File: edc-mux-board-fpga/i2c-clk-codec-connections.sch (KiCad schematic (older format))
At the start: 4 parts

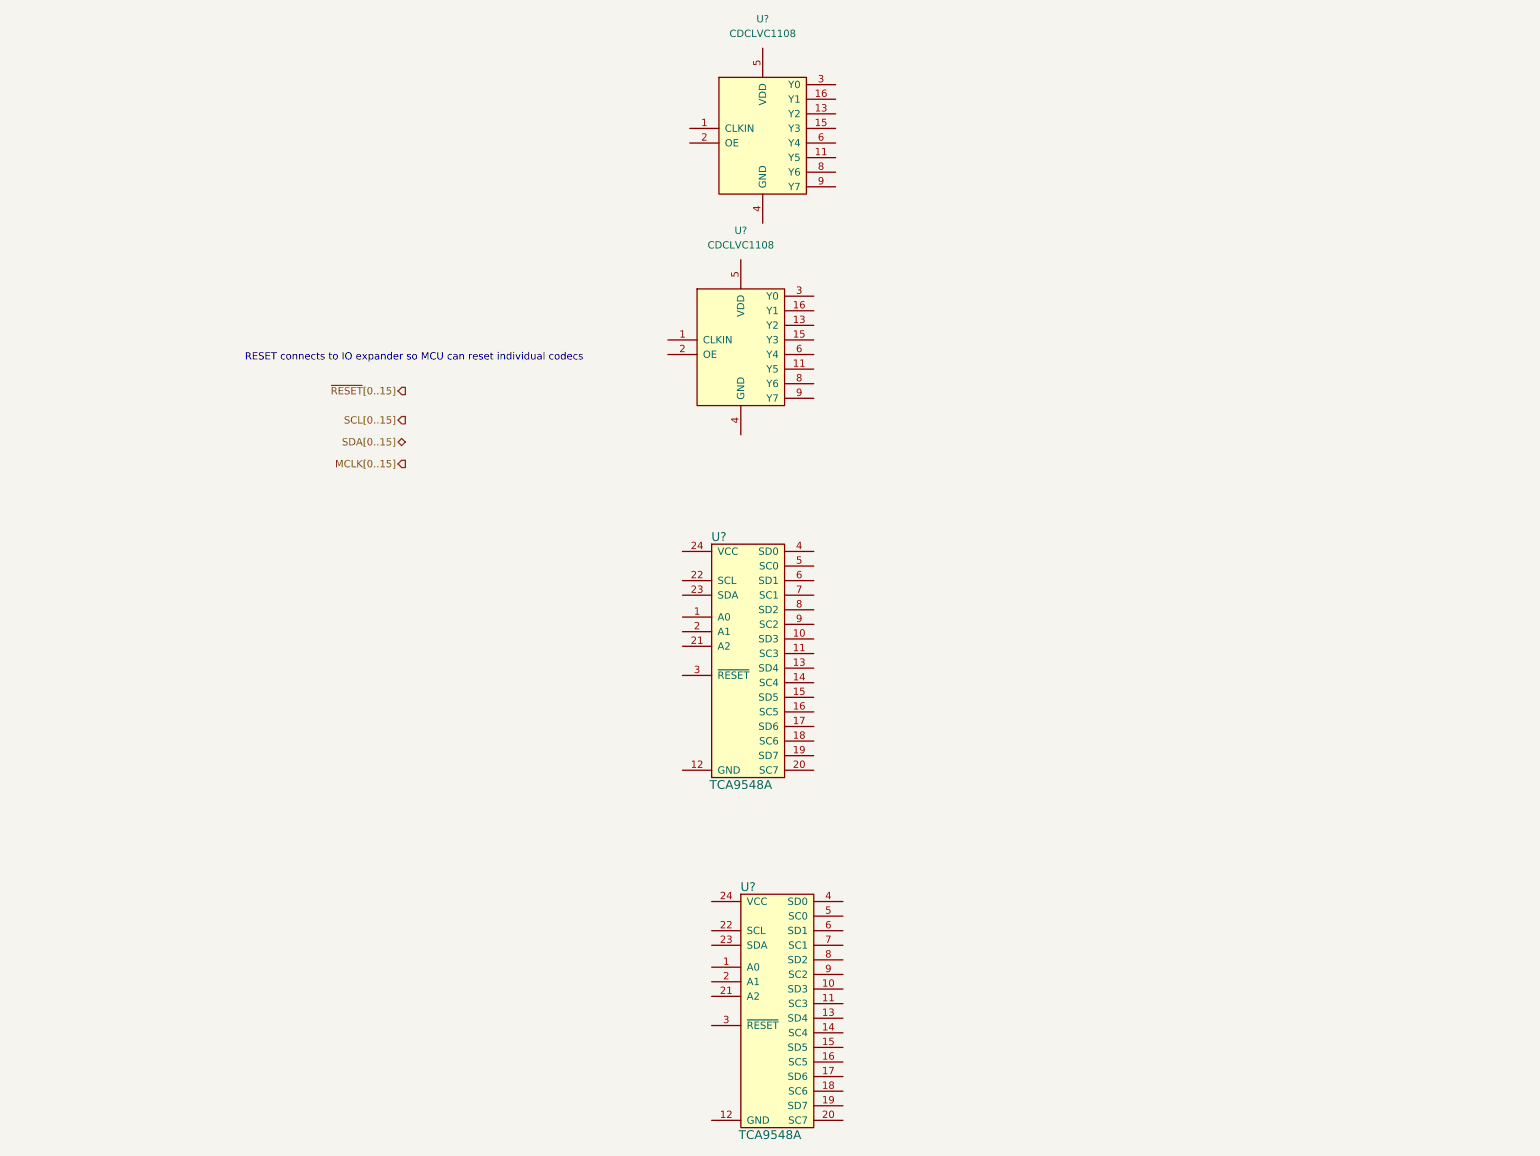
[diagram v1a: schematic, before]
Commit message: connected up mclks for codecs
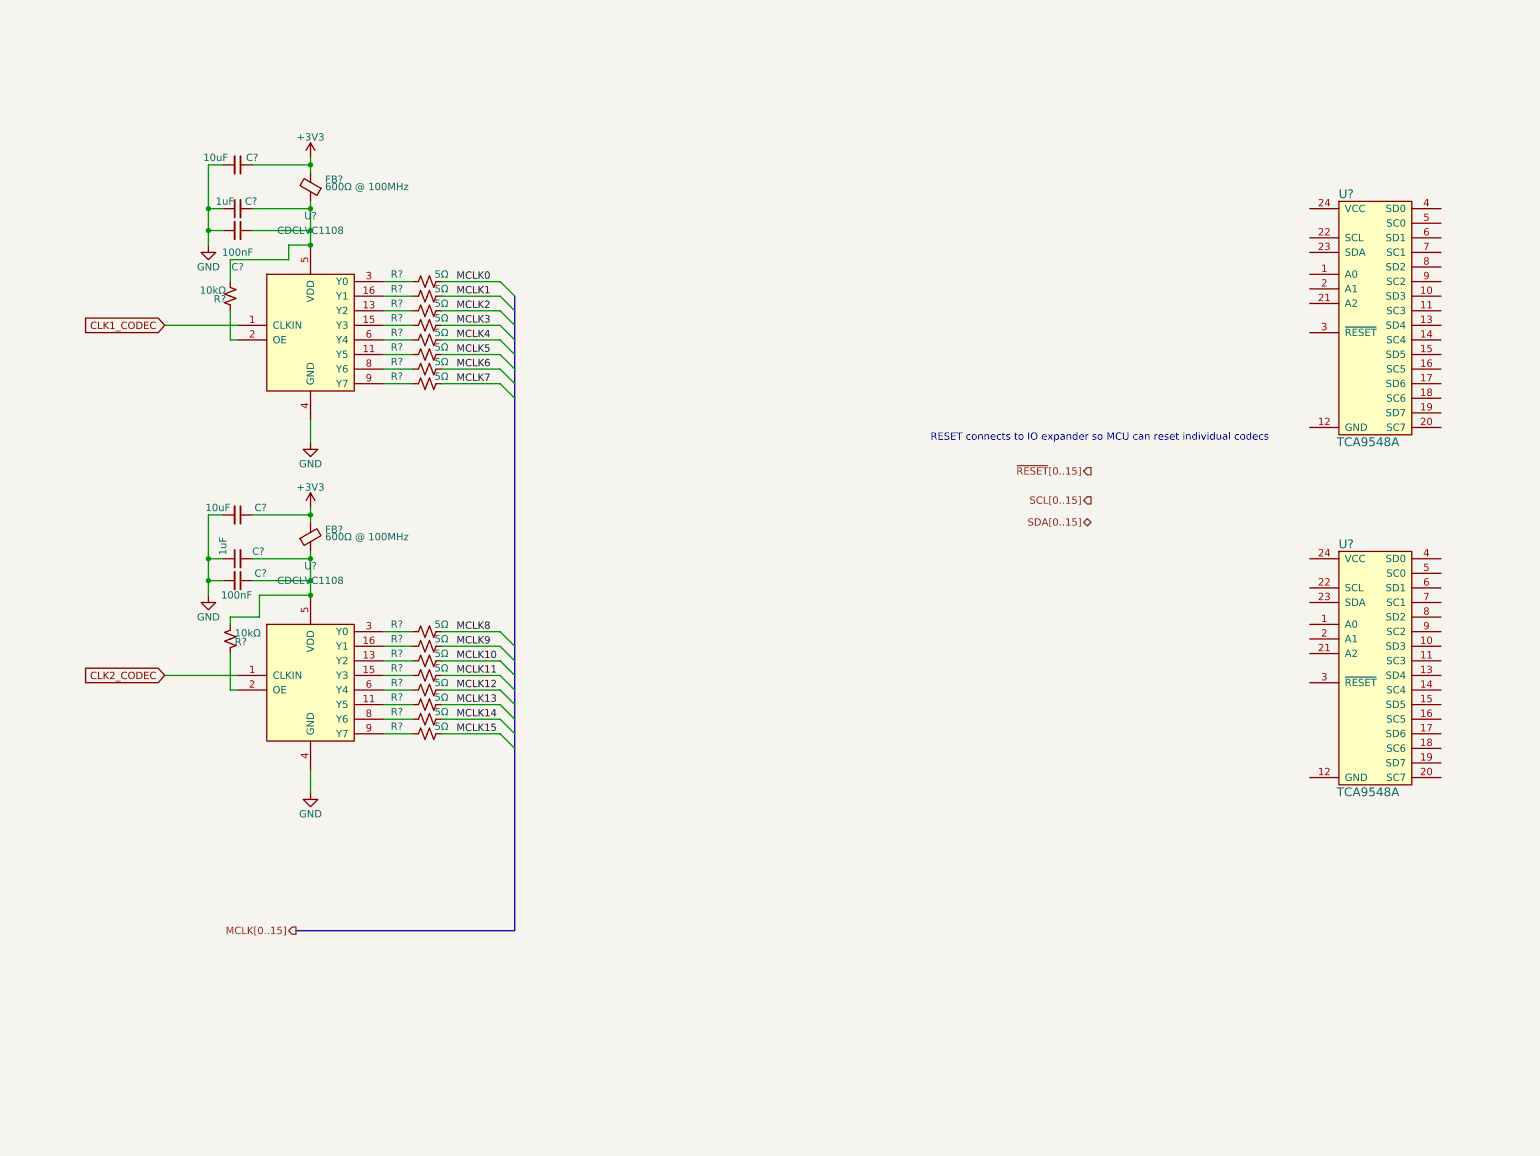
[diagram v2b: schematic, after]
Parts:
- added C? (x2): 1uF, Capacitor_SMD:C_0603_1608Metric, symbol Device:C_Small
- added C? (x2): 10uF, Capacitor_SMD:C_1206_3216Metric, symbol Device:C_Small
- added C? (x2): 100nF, Capacitor_SMD:C_0603_1608Metric, symbol Device:C_Small
- added FB? (x2): 600Ω @ 100MHz, Capacitor_SMD:C_0805_2012Metric, symbol Device:Ferrite_Bead_Small
- added R? (x2): 10kΩ, symbol Device:R_Small_US
- added R? (x16): 5Ω, symbol Device:R_Small_US
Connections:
- net CLK1_CODEC: now reaches U?.1 (CLKIN)
- net at U?.10 (VDD), U?.14 (VDD), U?.5 (VDD): now also C?.1, C?.2, FB?.1, R?.2 (x2)
- net at U?.11 (Y5): now also R?.2 (x2)
- net GND: now reaches U?.12 (GND), U?.4 (GND), U?.7 (GND)
- net GND: now also U?.12 (GND), U?.4 (GND), U?.7 (GND), C?.1, C?.1, C?.2, C?.2, C?.2, C?.2
- net at U?.13 (Y2): now also R?.2 (x2)
- net at U?.15 (Y3): now also R?.2 (x2)
- net at U?.16 (Y1): now also R?.2 (x2)
- net at U?.2 (OE): now also R?.1 (x2)
- net at U?.3 (Y0): now also R?.2 (x2)
- net at U?.6 (Y4): now also R?.2 (x2)
- net at U?.8 (Y6): now also R?.2 (x2)
- net at U?.9 (Y7): now also R?.2 (x2)
- net CLK2_CODEC: now reaches U?.1 (CLKIN)
- new net +3V3: C?.1, C?.1, FB?.2, FB?.2
- new net MCLK0: R?.1
- new net MCLK1: R?.1
- new net MCLK10: R?.1
- new net MCLK11: R?.1
- new net MCLK12: R?.1
- new net MCLK13: R?.1
- new net MCLK14: R?.1
- new net MCLK15: R?.1
- new net MCLK2: R?.1
- new net MCLK3: R?.1
- new net MCLK4: R?.1
- new net MCLK5: R?.1
- new net MCLK6: R?.1
- new net MCLK7: R?.1
- new net MCLK8: R?.1
- new net MCLK9: R?.1
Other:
- moved on the sheet: U?

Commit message: Finished CODEC and MCU interconnections
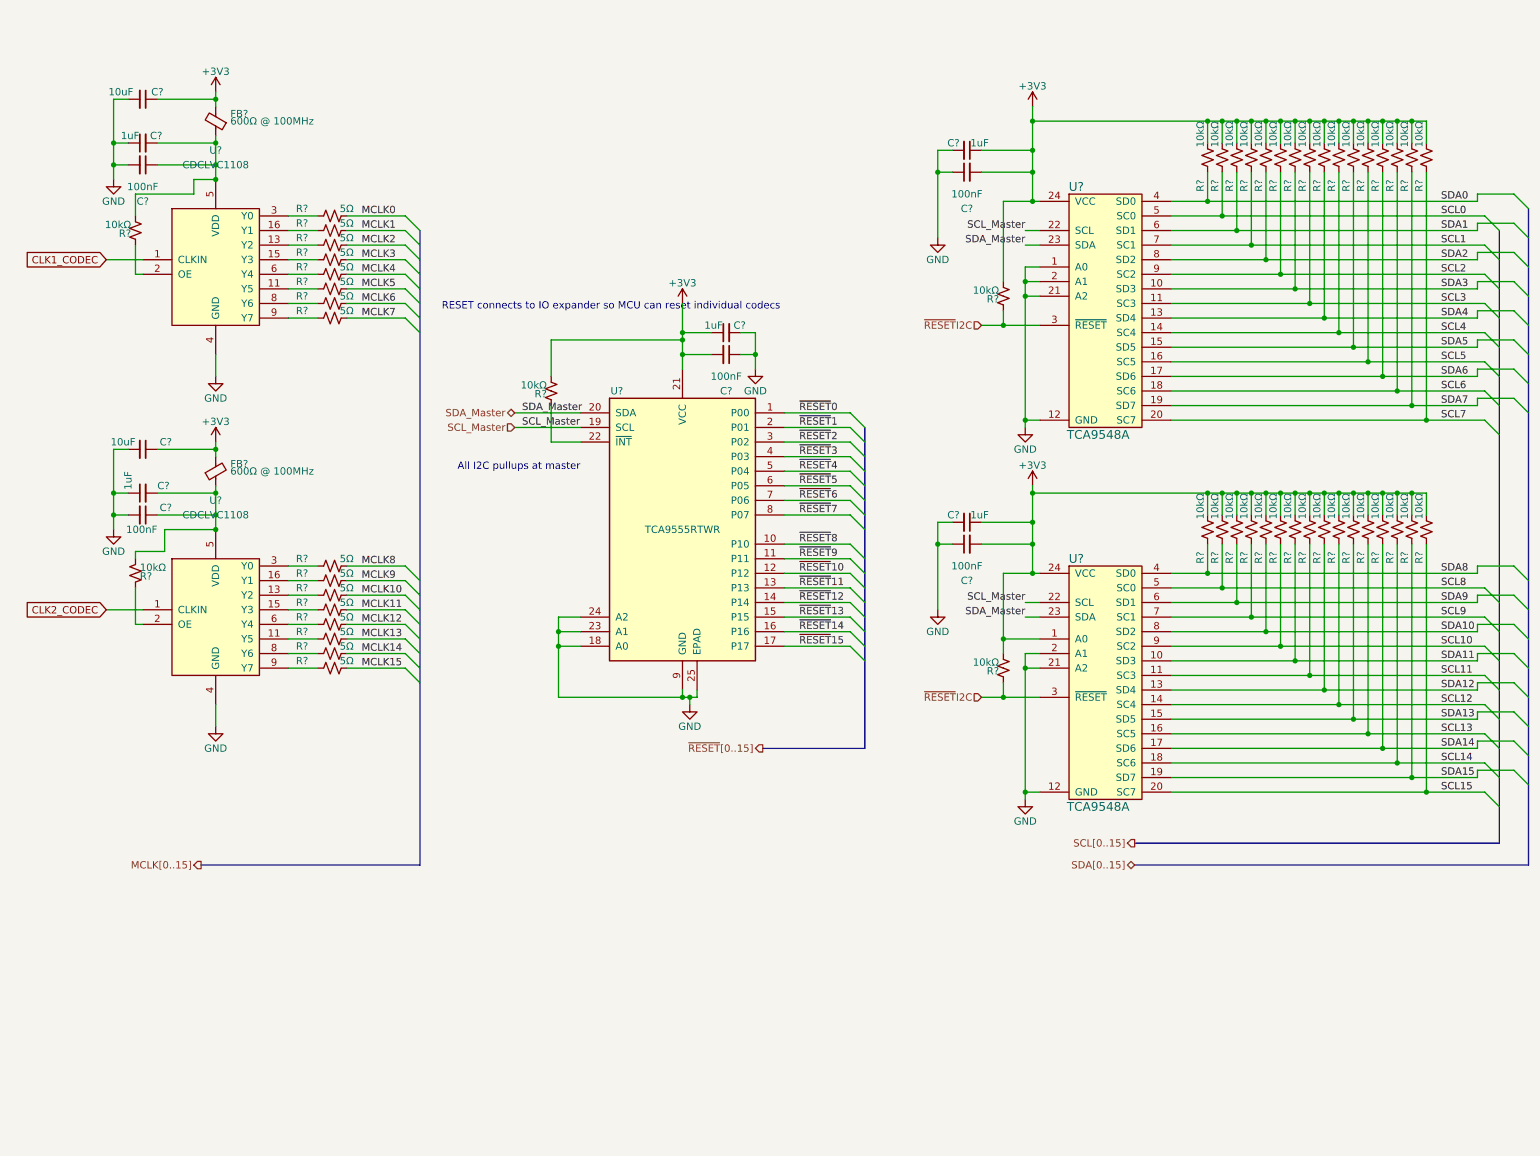
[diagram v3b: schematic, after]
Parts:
- added C? (x3): 100nF, Capacitor_SMD:C_0603_1608Metric, symbol Device:C_Small
- added C? (x3): 1uF, Capacitor_SMD:C_0603_1608Metric, symbol Device:C_Small
- added R? (x35): 10kΩ, symbol Device:R_Small_US
- added U?: TCA9555RTWR, Package_DFN_QFN:QFN-24-1EP_4x4mm_P0.5mm_EP2.6x2.6mm, symbol Interface_Expansion:TCA9555RTWR
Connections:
- net +3V3: now also U?.1 (A0), U?.24 (VCC), U?.24 (VCC), C?.1, C?.1, C?.1, C?.2, C?.2, C?.2, R?.2, R?.2, R?.2, R?.2, R?.2, R?.2, R?.2, R?.2, R?.2, R?.2, R?.2, R?.2, R?.2, R?.2, R?.2, R?.2, R?.2, R?.2, R?.2, R?.2, R?.2, R?.2, R?.2, R?.2, R?.2, R?.2, R?.2, R?.2, R?.2, R?.2, R?.2, R?.2, R?.2, R?.2, R?.2, U?.21 (VCC)
- net GND: now also U?.1 (A0), U?.12 (GND), U?.12 (GND), U?.2 (A1), U?.2 (A1), U?.21 (A2), U?.21 (A2), C?.1, C?.1, C?.1, C?.2, C?.2, C?.2, U?.18 (A0), U?.23 (A1), U?.24 (A2), U?.25 (EPAD), U?.9 (GND)
- net SDA3: now reaches U?.10 (SD3)
- net SDA3: now also R?.1
- net SCL3: now reaches U?.11 (SC3)
- net SCL3: now also R?.1
- net SDA4: now reaches U?.13 (SD4)
- net SDA4: now also R?.1
- net SCL4: now reaches U?.14 (SC4)
- net SCL4: now also R?.1
- net SDA5: now reaches U?.15 (SD5)
- net SDA5: now also R?.1
- net SCL5: now reaches U?.16 (SC5)
- net SCL5: now also R?.1
- net SDA6: now reaches U?.17 (SD6)
- net SDA6: now also R?.1
- net SCL6: now reaches U?.18 (SC6)
- net SCL6: now also R?.1
- net SDA7: now reaches U?.19 (SD7)
- net SDA7: now also R?.1
- net SCL7: now reaches U?.20 (SC7)
- net SCL7: now also R?.1
- net SCL_Master: now reaches U?.22 (SCL)
- net SCL_Master: now also U?.22 (SCL), U?.19 (SCL)
- net SDA_Master: now reaches U?.23 (SDA)
- net SDA_Master: now also U?.23 (SDA), U?.20 (SDA)
- net ~RESET~I2C: now reaches U?.3 (~RESET)
- net ~RESET~I2C: now also U?.3 (~RESET), R?.1, R?.1
- net SDA0: now reaches U?.4 (SD0)
- net SDA0: now also R?.1
- net SCL0: now reaches U?.5 (SC0)
- net SCL0: now also R?.1
- net SDA1: now reaches U?.6 (SD1)
- net SDA1: now also R?.1
- net SCL1: now reaches U?.7 (SC1)
- net SCL1: now also R?.1
- net SDA2: now reaches U?.8 (SD2)
- net SDA2: now also R?.1
- net SCL2: now reaches U?.9 (SC2)
- net SCL2: now also R?.1
- net SDA11: now reaches U?.10 (SD3)
- net SDA11: now also R?.1
- net SCL11: now reaches U?.11 (SC3)
- net SCL11: now also R?.1
- net SDA12: now reaches U?.13 (SD4)
- net SDA12: now also R?.1
- net SCL12: now reaches U?.14 (SC4)
- net SCL12: now also R?.1
- net SDA13: now reaches U?.15 (SD5)
- net SDA13: now also R?.1
- net SCL13: now reaches U?.16 (SC5)
- net SCL13: now also R?.1
- net SDA14: now reaches U?.17 (SD6)
- net SDA14: now also R?.1
- net SCL14: now reaches U?.18 (SC6)
- net SCL14: now also R?.1
- net SDA15: now reaches U?.19 (SD7)
- net SDA15: now also R?.1
- net SCL15: now reaches U?.20 (SC7)
- net SCL15: now also R?.1
- net SDA8: now reaches U?.4 (SD0)
- net SDA8: now also R?.1
- net SCL8: now reaches U?.5 (SC0)
- net SCL8: now also R?.1
- net SDA9: now reaches U?.6 (SD1)
- net SDA9: now also R?.1
- net SCL9: now reaches U?.7 (SC1)
- net SCL9: now also R?.1
- net SDA10: now reaches U?.8 (SD2)
- net SDA10: now also R?.1
- net SCL10: now reaches U?.9 (SC2)
- net SCL10: now also R?.1
- new net: R?.1, U?.22 (~INT)
- new net ~RESET~0: U?.1 (P00)
- new net ~RESET~1: U?.2 (P01)
- new net ~RESET~10: U?.12 (P12)
- new net ~RESET~11: U?.13 (P13)
- new net ~RESET~12: U?.14 (P14)
- new net ~RESET~13: U?.15 (P15)
- new net ~RESET~14: U?.16 (P16)
- new net ~RESET~15: U?.17 (P17)
- new net ~RESET~2: U?.3 (P02)
- new net ~RESET~3: U?.4 (P03)
- new net ~RESET~4: U?.5 (P04)
- new net ~RESET~5: U?.6 (P05)
- new net ~RESET~6: U?.7 (P06)
- new net ~RESET~7: U?.8 (P07)
- new net ~RESET~8: U?.10 (P10)
- new net ~RESET~9: U?.11 (P11)
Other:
- note added: "All I2C pullups at master"
- moved on the sheet: C?, FB?, R?, U?

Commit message: Finished FPGA and MCU interconnections.
Finished up interrupt wiring
Fixed a few missing connections
Annotated Schematic
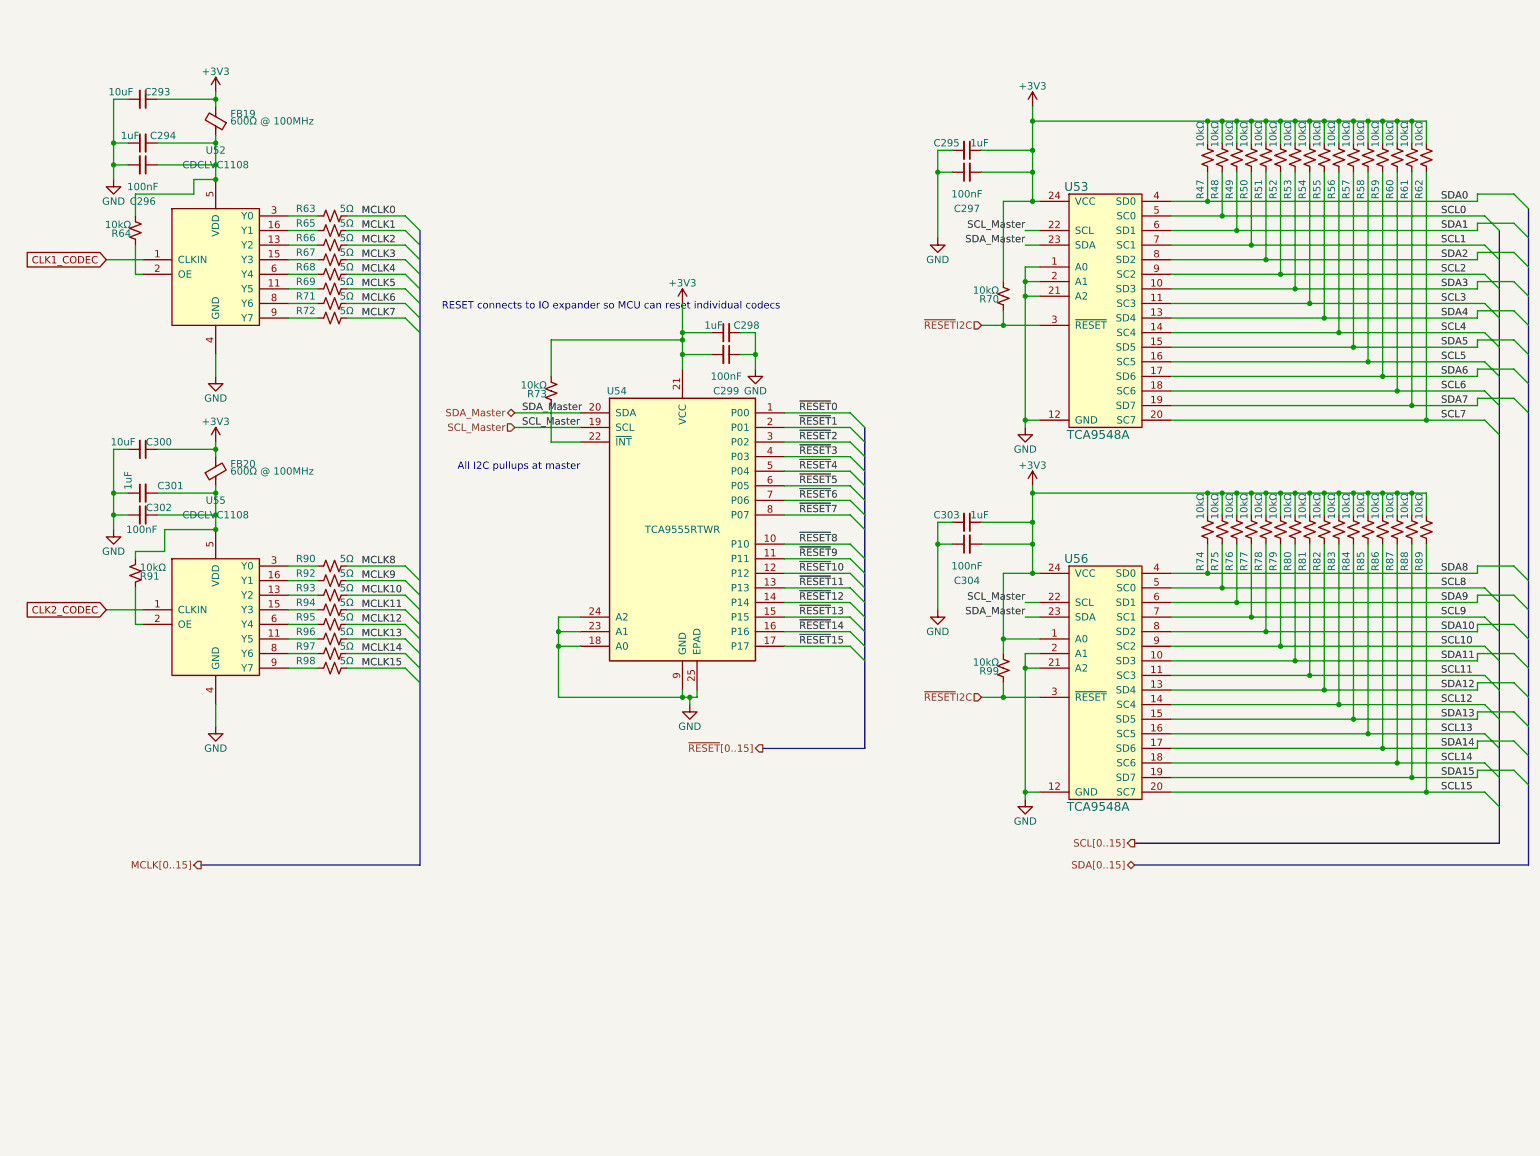
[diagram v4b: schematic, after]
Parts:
- gave numbers to parts that had none: 72
